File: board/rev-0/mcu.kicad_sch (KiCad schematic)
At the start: 29 parts, among them J1 I2C, J2 Conn_01x08, J3 USB_C_Receptacle_USB2.0_16P, J4 UART, U1 ESP32-S3-WROOM-1

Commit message: Added lib
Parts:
- J1, J4: footprint CONN_A-6373-03A_MOL -> 022232031:CONN_A-6373-03A_MOL
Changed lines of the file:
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@@
 			)
 		)
-		(property "Footprint" "CONN_A-6373-03A_MOL"
+		(property "Footprint" "022232031:CONN_A-6373-03A_MOL"
 			(at 439.42 175.26 0)
 			(effects
@@
 			)
 		)
-		(property "Footprint" "CONN_A-6373-03A_MOL"
+		(property "Footprint" "022232031:CONN_A-6373-03A_MOL"
 			(at 152.4 200.66 0)
 			(effects

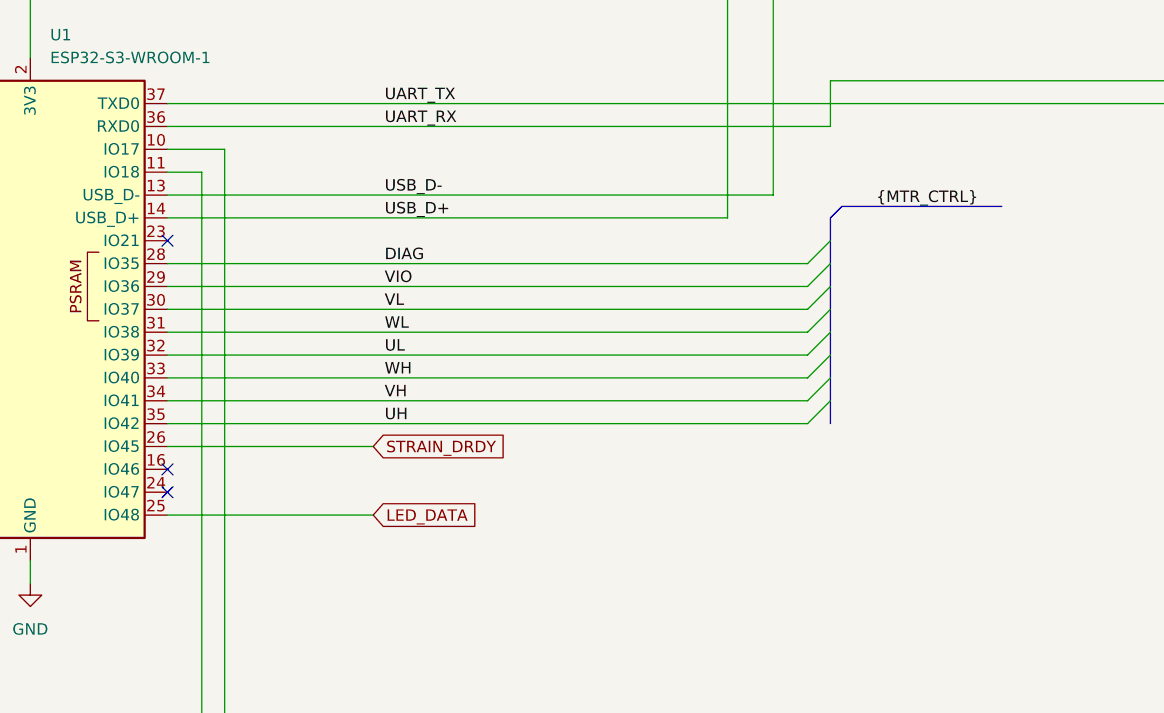
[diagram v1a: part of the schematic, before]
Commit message: Changed PSRAM pins
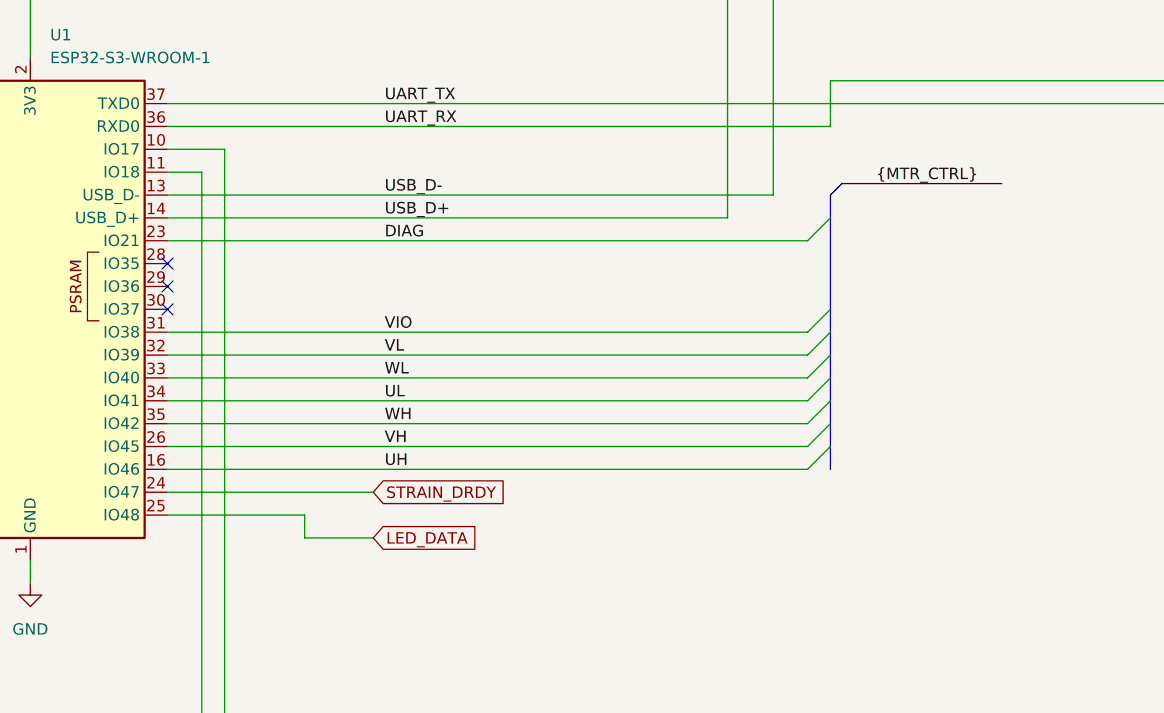
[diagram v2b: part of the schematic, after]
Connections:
- net DIAG: now also U1.23 (IO21); no longer U1.28 (IO35)
- net STRAIN_DRDY: now also U1.24 (IO47); no longer U1.26 (IO45)
- net UH: now also U1.16 (IO46); no longer U1.35 (IO42)
- net UL: now also U1.34 (IO41); no longer U1.32 (IO39)
- net VH: now also U1.26 (IO45); no longer U1.34 (IO41)
- net VIO: now also U1.31 (IO38); no longer U1.29 (IO36)
- net VL: now also U1.32 (IO39); no longer U1.30 (IO37)
- net WH: now also U1.35 (IO42); no longer U1.33 (IO40)
- net WL: now also U1.33 (IO40); no longer U1.31 (IO38)

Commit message: Added I2C pullups and LCD net labels
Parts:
- added R16, R17: R_US, symbol Device:R_US
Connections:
- net SCL: now also R16.2
- net SDA: now also R17.2
- net VCC_3V3: now also R16.1, R17.1
- net LCD_RST: now reaches J2.3 (Pin_3), U1.7 (IO7)
- net LCD_SCK: now reaches J2.4 (Pin_4), U1.8 (IO15)
- net LCD_DATA: now reaches J2.5 (Pin_5), U1.9 (IO16)
- net LCD_BL: now reaches J2.6 (Pin_6), U1.10 (IO17)
- net LCD_CS: now reaches J2.7 (Pin_7), U1.11 (IO18)
- net LCD_CMD: now reaches J2.8 (Pin_8), U1.12 (IO8)

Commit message: Added key LEDs
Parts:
- added LED1, LED2, LED3, LED4, LED5, LED6, LED7, LED8, LED9: IN-PI55TATPRPGPB, LED_IN-PI55TAT_INL:LED_IN-PI55TAT_INL, symbol my_lib:IN-PI55TATPRPGPB
- added R18: 500, symbol Device:R_US
- added U7: SN74LV1T34DBV, Package_TO_SOT_SMD:SOT-23-5, symbol Logic_LevelTranslator:SN74LV1T34DBV
- R16, R17: value R_US -> 10K
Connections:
- net GND: now also LED1.1 (GND), LED2.1 (GND), LED3.1 (GND), LED4.1 (GND), LED5.1 (GND), LED6.1 (GND), LED7.1 (GND), LED8.1 (GND), LED9.1 (GND), U7.3 (GND)
- net KEY_LED_DATA: now reaches U1.15 (IO3)
- net KEY_LED_DATA: now also U7.2 (A)
- net LED_DATA renamed DIAL_LED_DATA
- new net: R18.1, U7.4 (Y)
- new net: LED5.2 (DOUT), LED6.3 (DIN)
- new net: LED4.2 (DOUT), LED5.3 (DIN)
- new net: LED6.2 (DOUT), LED7.3 (DIN)
- new net: LED3.2 (DOUT), LED4.3 (DIN)
- new net: LED2.2 (DOUT), LED3.3 (DIN)
- new net: LED1.2 (DOUT), LED2.3 (DIN)
- new net: LED8.2 (DOUT), LED9.3 (DIN)
- new net: LED7.2 (DOUT), LED8.3 (DIN)
- new net: LED1.3 (DIN), R18.2
- new net VCC_5V: LED1.4 (VDD), LED2.4 (VDD), LED3.4 (VDD), LED4.4 (VDD), LED5.4 (VDD), LED6.4 (VDD), LED7.4 (VDD), LED8.4 (VDD), LED9.4 (VDD), U7.5 (VCC)

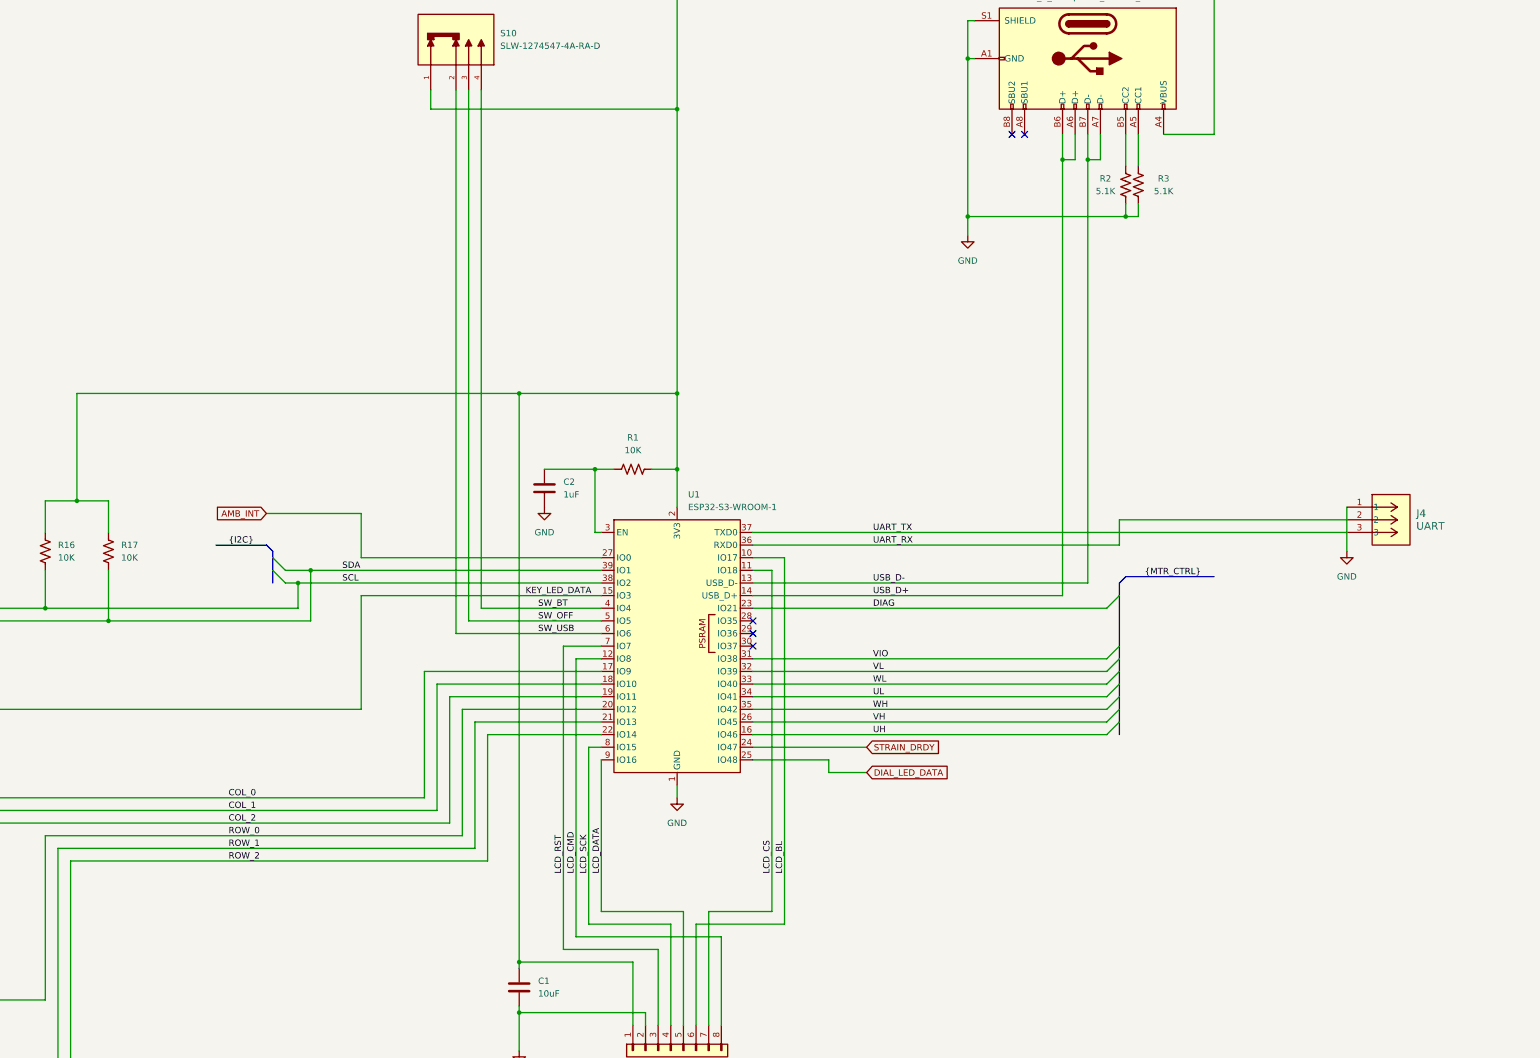
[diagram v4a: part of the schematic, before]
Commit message: Added strapping GPIO pull-up/-down options, replaced UART breakout with charging status signals
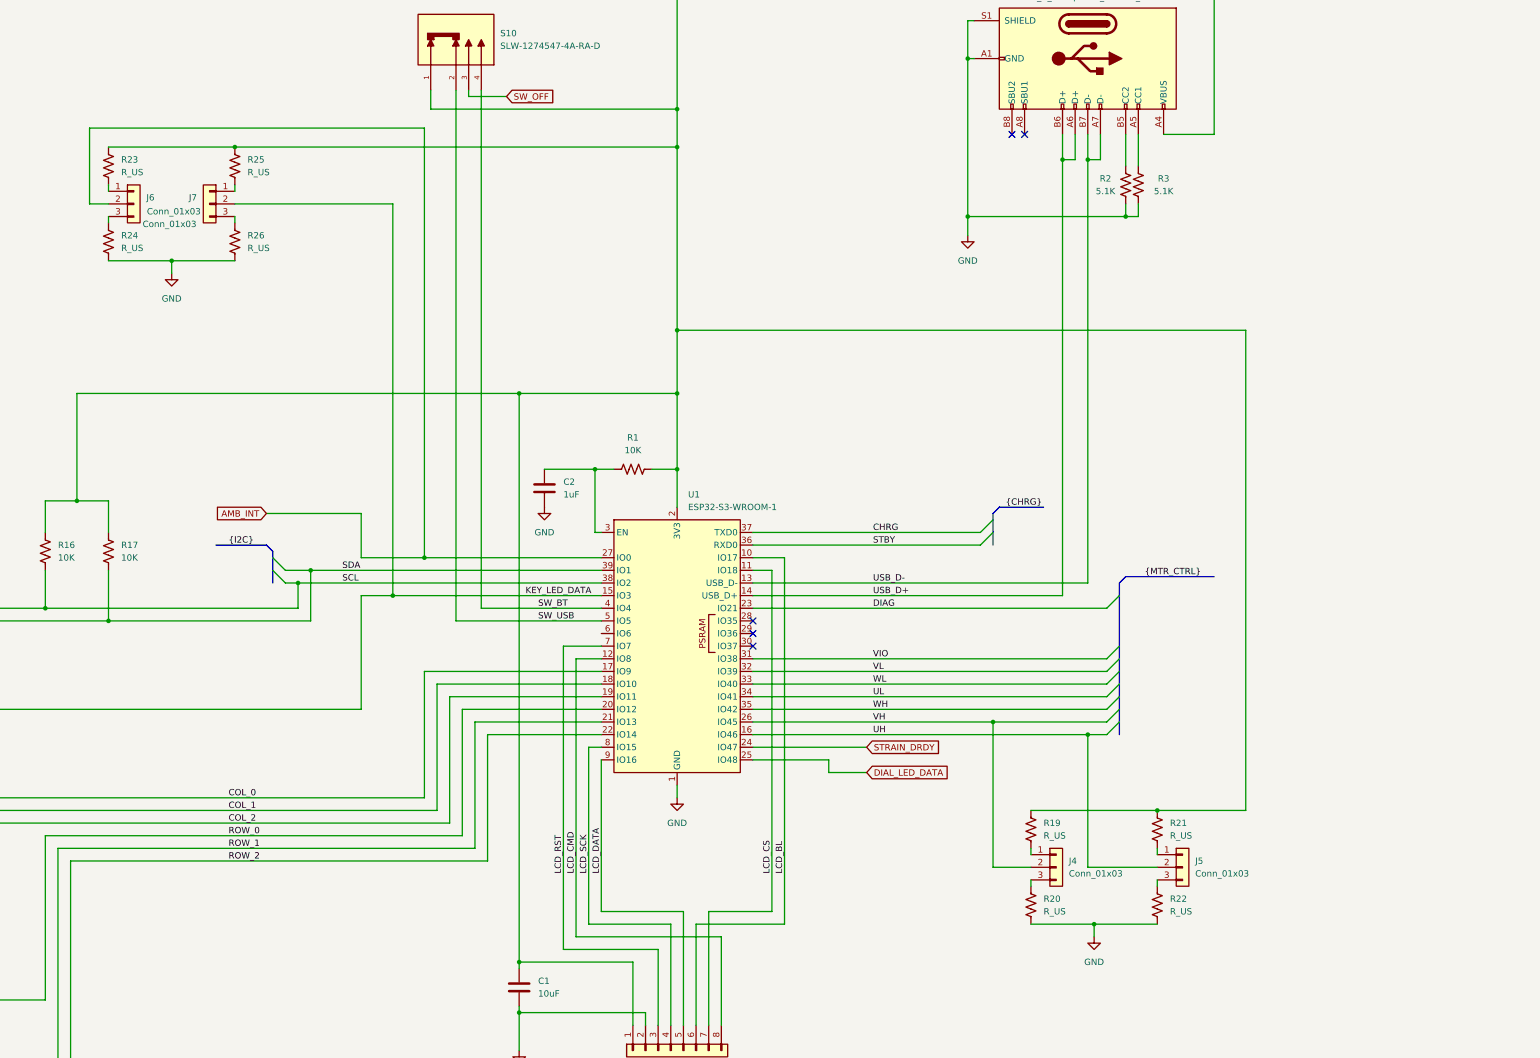
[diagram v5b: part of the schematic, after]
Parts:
- removed J4: UART, 022232031:CONN_A-6373-03A_MOL, symbol my_lib:22232031
- added J4, J5, J6, J7: Conn_01x03, symbol Connector_Generic:Conn_01x03
- added R19, R20, R21, R22, R23, R24, R25, R26: R_US, symbol Device:R_US
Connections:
- net AMB_INT: now also J6.2 (Pin_2)
- net GND: now also R20.2, R22.2, R24.2, R26.2
- net KEY_LED_DATA: now also J7.2 (Pin_2)
- net SW_OFF: no longer U1.5 (IO5)
- net SW_USB: now also U1.5 (IO5); no longer U1.6 (IO6)
- net UH: now also J5.2 (Pin_2)
- net VCC_3V3: now also R19.1, R21.1, R23.1, R25.1
- net VH: now also J4.2 (Pin_2)
- net UART_RX renamed STBY
- net UART_TX renamed CHRG
- new net: J6.3 (Pin_3), R24.1
- new net: J5.1 (Pin_1), R21.2
- new net: J5.3 (Pin_3), R22.1
- new net: J4.3 (Pin_3), R20.1
- new net: J7.1 (Pin_1), R25.2
- new net: J7.3 (Pin_3), R26.1
- new net: J4.1 (Pin_1), R19.2
- new net: J6.1 (Pin_1), R23.2

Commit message: Updated pdf
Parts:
- R19, R20, R21, R22, R23, R24, R25, R26: value R_US -> 10K
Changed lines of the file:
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@@
 			)
 		)
-		(property "Value" "R_US"
+		(property "Value" "10K"
 			(at 193.04 123.1899 0)
 			(effects
@@
 			)
 		)
-		(property "Value" "R_US"
+		(property "Value" "10K"
 			(at 403.86 241.2999 0)
 			(effects
@@
 			)
 		)
-		(property "Value" "R_US"
+		(property "Value" "10K"
 			(at 403.86 256.5399 0)
 			(effects
@@
 			)
 		)
-		(property "Value" "R_US"
+		(property "Value" "10K"
 			(at 378.46 256.5399 0)
 			(effects
@@
 			)
 		)
-		(property "Value" "R_US"
+		(property "Value" "10K"
 			(at 218.44 107.9499 0)
 			(effects
@@
 			)
 		)
-		(property "Value" "R_US"
+		(property "Value" "10K"
 			(at 218.44 123.1899 0)
 			(effects
@@
 			)
 		)
-		(property "Value" "R_US"
+		(property "Value" "10K"
 			(at 193.04 107.9499 0)
 			(effects
@@
 			)
 		)
-		(property "Value" "R_US"
+		(property "Value" "10K"
 			(at 378.46 241.2999 0)
 			(effects
